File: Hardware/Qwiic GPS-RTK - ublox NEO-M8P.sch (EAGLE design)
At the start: 53 parts, among them J13 U.FL, J3 PTH, U1 NEO-M8P, U2 3.3V

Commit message: Adding examples
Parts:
- removed JP11: SPI, SparkFun-Connectors:M06NO_SILK_FEMALE_PTH
- added J1: (no value), SparkFun-Connectors:CONN_07NO_SILK
- D1: value BLUE -> Yellow; device SparkFun-LED:LED-BLUE0603 -> SparkFun-LED:LED-YELLOW0603
- JP15: value SPI -> (none)
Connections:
- net 3.3V: now also J1.3; no longer JP11.2
- net 5V: now also J1.2
- net GND: now also J1.1; no longer JP11.1
- net RXI/MOSI: now also J1.5; no longer JP11.4
- net SCL/SCK: now also J1.7; no longer JP11.6
- net SDA/!CS: now also J1.4; no longer JP11.3
- net TXO/MISO: now also J1.6; no longer JP11.5
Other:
- note added: "7-bit unshifted I2C address: 0x42"
- note removed: "7-bit unshifted I2C address: 0x??"
- note removed: "Is VCC_USB on ESD wired correctly?"
- note removed: "SMA connector instead of ufl?"
- moved on the sheet: D5, J6

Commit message: Fix schematic typo
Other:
- note added: "Cut jumper to disable LED"
- note removed: "Cut jumper to disable PPS LED"
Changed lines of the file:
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@@
 I2C pullups from bus</text>
 <text x="19.558" y="73.914" size="1.778" layer="97">Cut jumper to
-disable PPS LED</text>
+disable LED</text>
 <text x="198.12" y="121.92" size="1.778" layer="97">Close Jumper to
 enable SPI</text>

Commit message: Modifications for reds.
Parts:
- removed U$31: SPARKX-LOGO3, SparkX:SPARKX-LOGO3
- added LOGO2: SFE_LOGO_NAME_FLAME.1_INCH, SparkFun-Aesthetics:SFE_LOGO_NAME_FLAME.1_INCH
- renumbered JP51 to JP5
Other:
- note added: "Close jumper to enable SPI"
- note added: "Cut jumper to remove I2C pullups from bus"
- note removed: "Close Jumper to enable SPI"
- note removed: "Cut JP5 to remove I2C pullups from bus"
- moved on the sheet: C4, C5, C6, D5, J6, U2

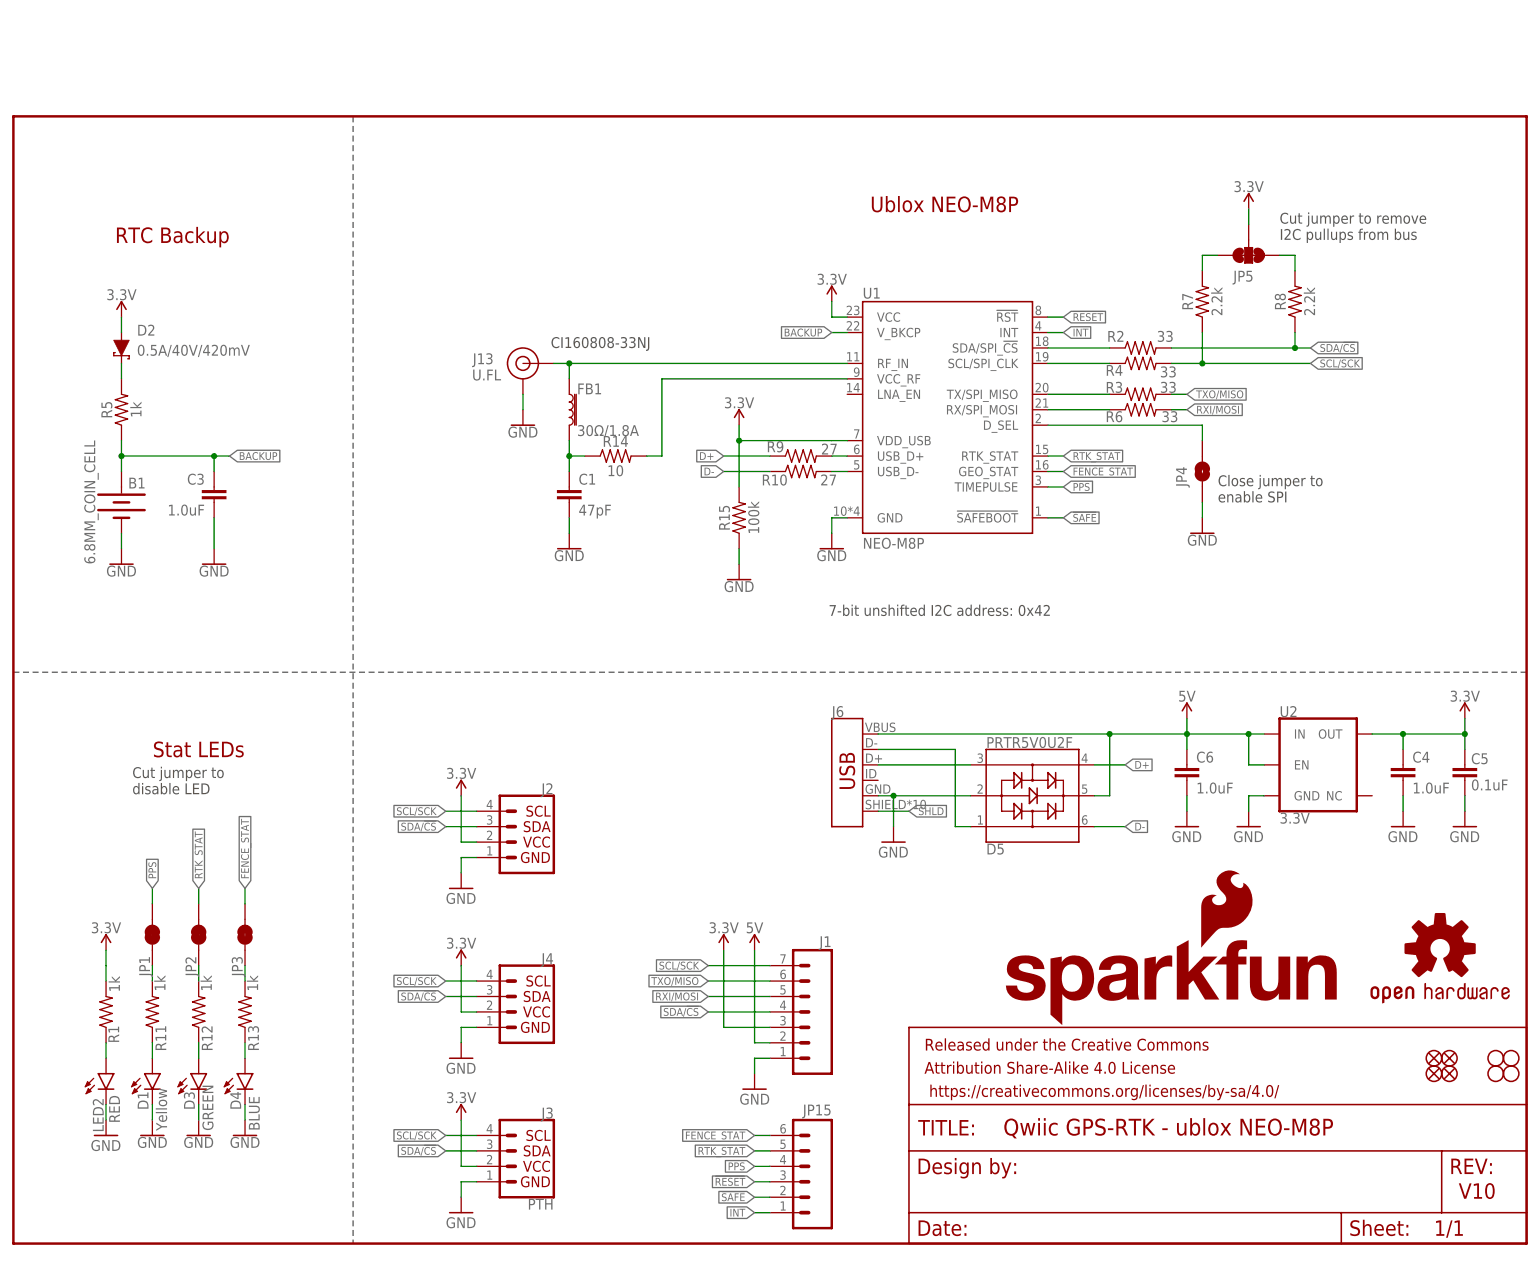
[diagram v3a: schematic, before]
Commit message: Adds reflowable battery and moves all parts to use SparkFun Libraries
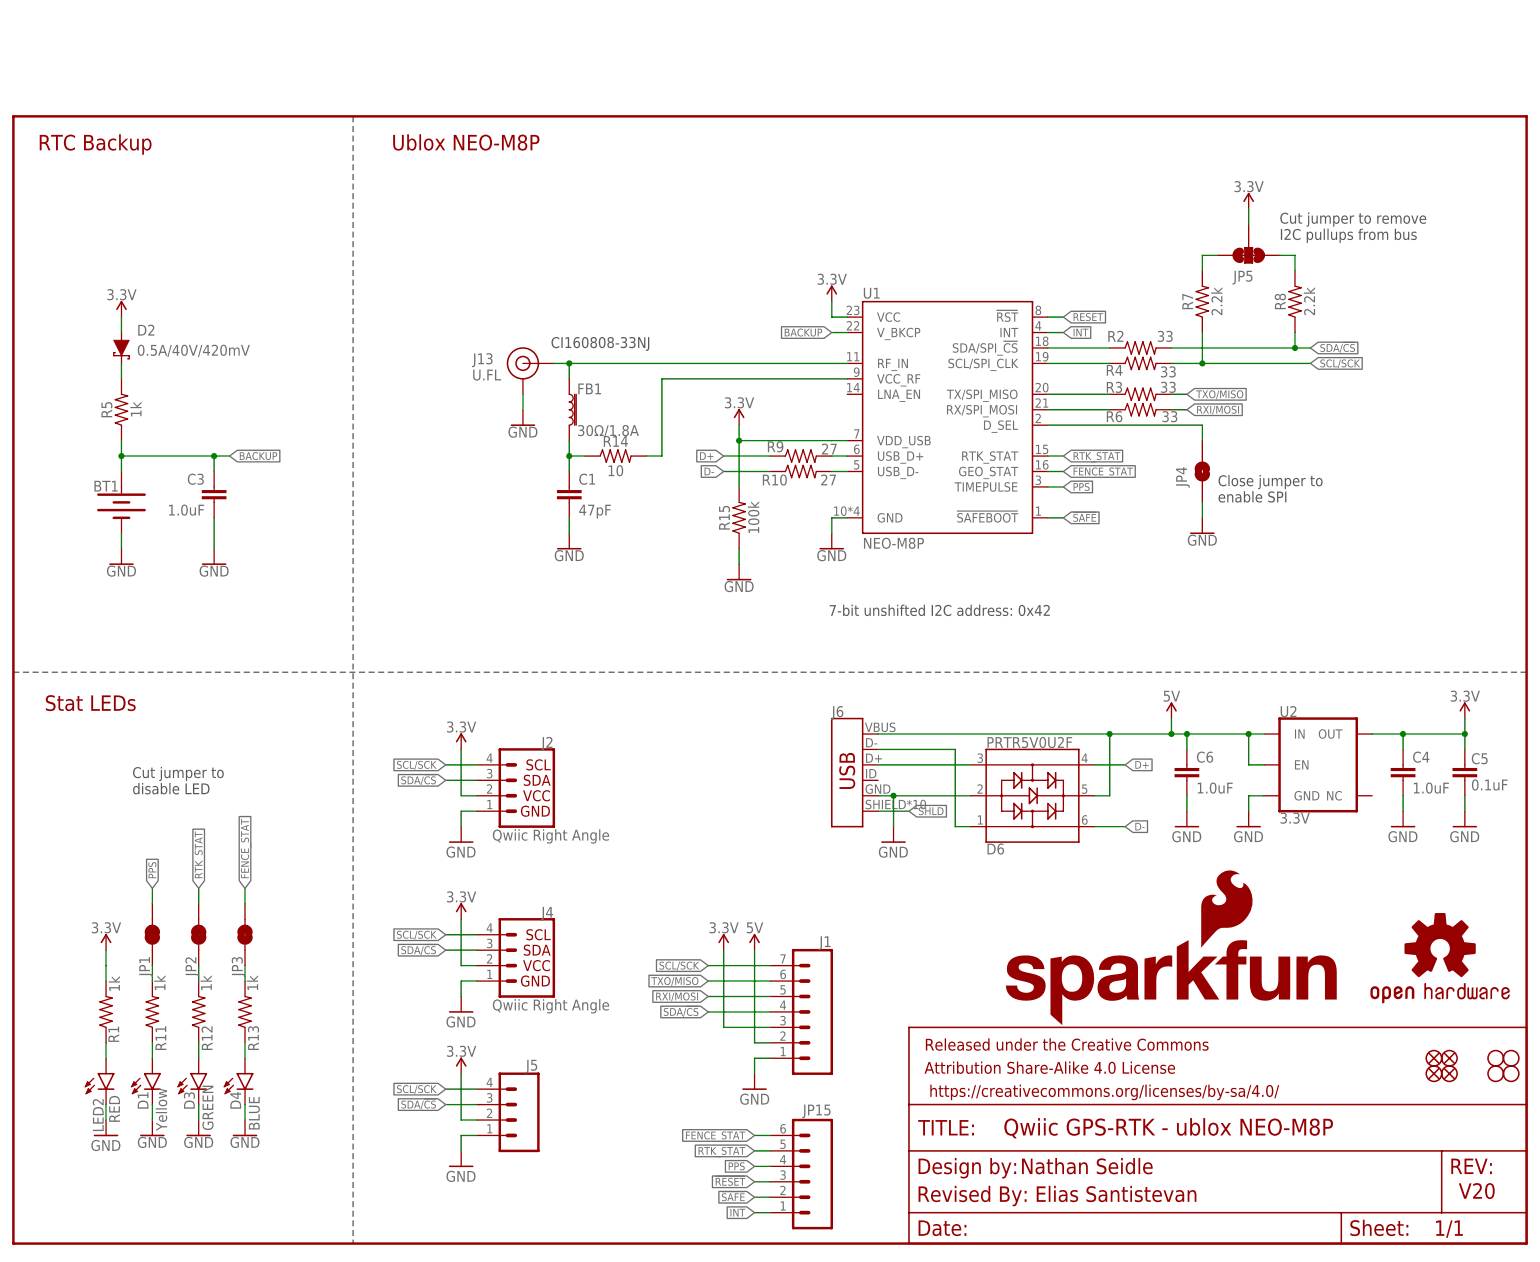
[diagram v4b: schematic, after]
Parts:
- removed B1: 6.8MM_COIN_CELL, SparkFun-Batteries:BATTERY-6.8MM_SMD
- removed D5: PRTR5V0U2F, funbit:PRTR5V0U2F
- removed J3: PTH, SparkX:I2C_STANDARD_NO_SILK
- added BT1: ML414H_IV01E_BATTERY, SparkFun-Batteries:ML414H_IV01E_BATTERY
- added D6: PRTR5V0U2F, SparkFun-IC-Power:PRTR5V0U2F
- added J5: (no value), SparkFun-Connectors:CONN_041X04_NO_SILK
- J2, J4: value (none) -> Qwiic Right Angle
- JP101, JP31, JP41, JP91: value STAND-OFF -> STAND-OFFTIGHT; device SparkFun:STAND-OFF -> SparkFun-Hardware:STAND-OFFTIGHT
- JP21, JP61, JP71, JP81: device SparkFun:FIDUCIALUFIDUCIAL -> SparkFun-Aesthetics:FIDUCIALUFIDUCIAL
- U1: device NEO-M8P:NEO-M8PM8P -> SparkFun-GPS:NEO-M8PM8P
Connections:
- net 3.3V: now also J5.2; no longer J3.VCC
- net 5V: now also D6.5; no longer D5.5
- net BACKUP: now also BT1.+; no longer B1.+
- net D+: now also D6.4; no longer D5.4
- net D-: now also D6.6; no longer D5.6
- net GND: now also BT1.-, D6.2, J5.1; no longer B1.-, D5.2, J3.GND
- net SCL/SCK: now also J5.4; no longer J3.SCL
- net SDA/!CS: now also J5.3; no longer J3.SDA
- net USB_D+: now also D6.3; no longer D5.3
- net USB_D-: now also D6.1; no longer D5.1
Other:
- note added: "Nathan Seidle"
- note added: "Revised By: Elias Santistevan"
- note added: "V20"
- note removed: "V10"
- moved on the sheet: J2, J4
